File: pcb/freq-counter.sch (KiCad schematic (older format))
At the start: 52 parts, among them J1 RPM, J2 BNC, J3 for RPM, Q1 CSC388A, Q2 CSC388A, Q3 2SA1015, Q4 2SC1815, Q5 2SC1815, SW1 SW_SPDT, SW2 SW_Push, SW3 SW_Push, U1 SN74HC02N, U2 ATTINY4313-PU(freq-counter), U3 EE-SX460, Y1 10MHz

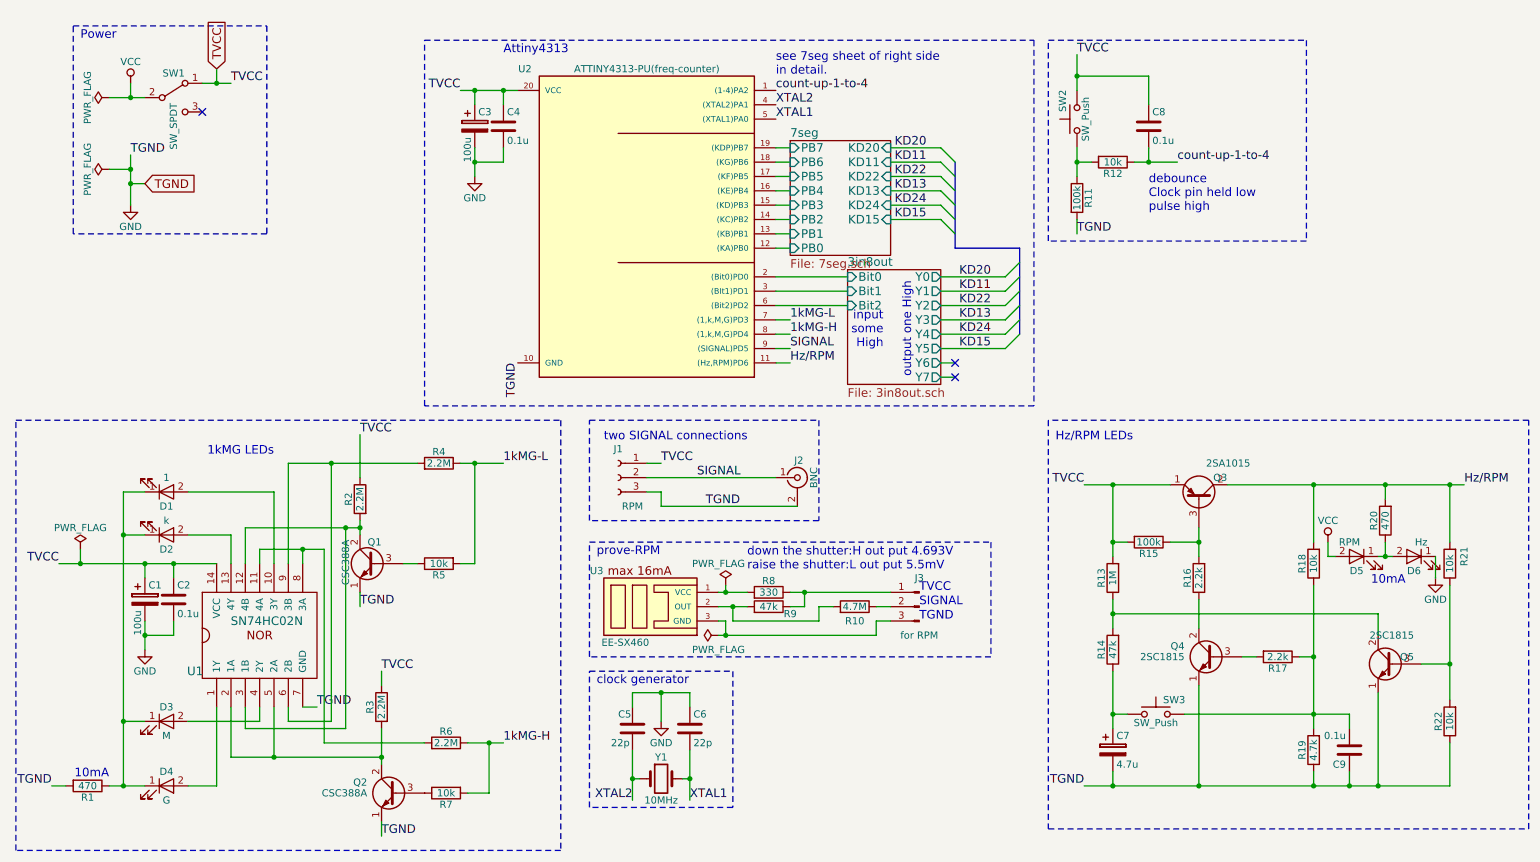
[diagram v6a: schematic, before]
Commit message: CvPcb で main 基板に部品を割り当てた。
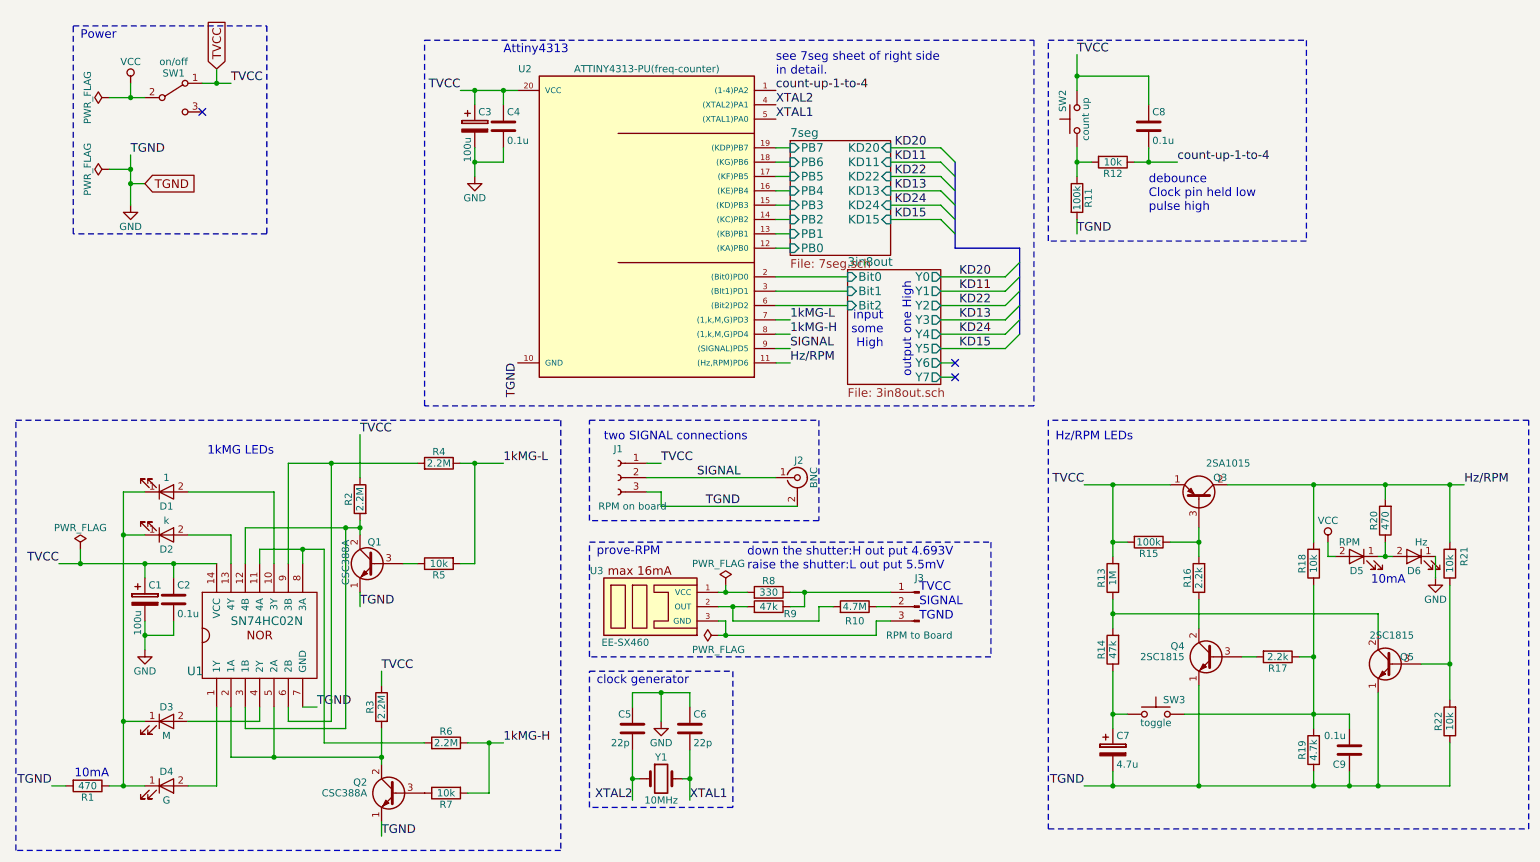
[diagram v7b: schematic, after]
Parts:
- C1, C3, C7: footprint (none) -> Capacitors_THT:CP_Radial_D5.0mm_P2.00mm
- C2, C4, C8, C9: footprint (none) -> Capacitors_THT:C_Disc_D3.4mm_W2.1mm_P2.50mm
- C5, C6: footprint (none) -> Capacitors_THT:C_Disc_D3.0mm_W1.6mm_P2.50mm
- D1, D2, D3, D4, D5, D6: footprint (none) -> LEDs:LED_D5.0mm
- J1: value RPM -> RPM on board; footprint (none) -> Connectors_JST:JST_XH_B03B-XH-A_03x2.50mm_Straight
- J2: footprint (none) -> Connectors_TE-Connectivity:BNC_Socket_TYCO-AMP
- J3: value for RPM -> RPM to Board; footprint (none) -> Connectors_JST:JST_XH_B03B-XH-A_03x2.50mm_Straight
- R1, R10, R11, R12, R13, R14, R15, R16, R17, R18, R19, R2, R20, R21, R22, R3, R4, R5, R6, R7, R8, R9: footprint (none) -> Resistors_THT:R_Axial_DIN0207_L6.3mm_D2.5mm_P7.62mm_Horizontal
- SW1: value SW_SPDT -> on/off; footprint (none) -> freq-counter:Slide-switch
- SW2: value SW_Push -> count up; footprint (none) -> freq-counter:TVDT18-tactile-switch
- SW3: value SW_Push -> toggle; footprint (none) -> freq-counter:TVDT18-tactile-switch
- U1: footprint (none) -> Housings_DIP:DIP-14_W7.62mm
- U3: footprint 3PIN_W30_D11_H8mm -> freq-counter:EE-SX460-P1
- Y1: footprint (none) -> Crystals:Crystal_HC49-4H_Vertical

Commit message: 変更点多し。
修正は色々よ。色々。
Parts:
- added J4: Jack-DC, Connectors:BARREL_JACK, symbol Jack-DC
- C1, C3, C7: footprint Capacitors_THT:CP_Radial_D5.0mm_P2.00mm -> Capacitors_THT:CP_Radial_D5.0mm_P2.50mm
- Q1, Q2, Q3, Q4, Q5: footprint TO_SOT_Packages_THT:TO-92_Molded_Narrow -> TO_SOT_Packages_THT:TO-92_Inline_Wide
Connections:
- net 1kMG-H: now also U2.7 ((1,k,M,G)PD3)
- net 1kMG-L: no longer U2.7 ((1,k,M,G)PD3)
- net GND: now also J1.1 (Pin_1), J4.2; no longer J1.3 (Pin_3)
- net Hz/RPM: now also U2.1 ((1-4)PA2); no longer U2.11 ((Hz,RPM)PD6)
- net SIGNAL: now also J1.3 (Pin_3); no longer J1.2 (Pin_2)
- net VCC: now also C1.1, C2.1, C3.1, C4.1, C8.1, J1.2 (Pin_2), Q3.1 (E), R13.2, R15.2, R2.1, R3.1, SW1.1 (A), SW2.2, U1.14 (VCC), U2.20 (VCC); no longer SW1.2 (B)
- net count-up-1-to-4: now also U2.11 ((Hz,RPM)PD6); no longer U2.1 ((1-4)PA2)
- net at R8.1, R9.1: now also J3.2 (Pin_2); no longer J3.1 (Pin_1)
- net at R10.1: now also J3.3 (Pin_3); no longer J3.2 (Pin_2)
- net at U3.3 (GND): now also J3.1 (Pin_1); no longer J3.3 (Pin_3)
- removed net TVCC: C1.1, C2.1, C3.1, C4.1, C8.1, J1.1 (Pin_1), Q3.1 (E), R13.2, R15.2, R2.1, R3.1, SW1.1 (A), SW2.2, U1.14 (VCC), U2.20 (VCC)
- new net: J4.1, SW1.2 (B)
- no-connect marks 3 -> 4
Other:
- note added: "5V Battery"
- moved on the sheet: R10
